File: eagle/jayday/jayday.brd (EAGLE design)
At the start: 120 x 80 mm, 35 parts, among them IC1 TPS2115, X1 2X5_1.27MM, X17 DX2R005HN2E700

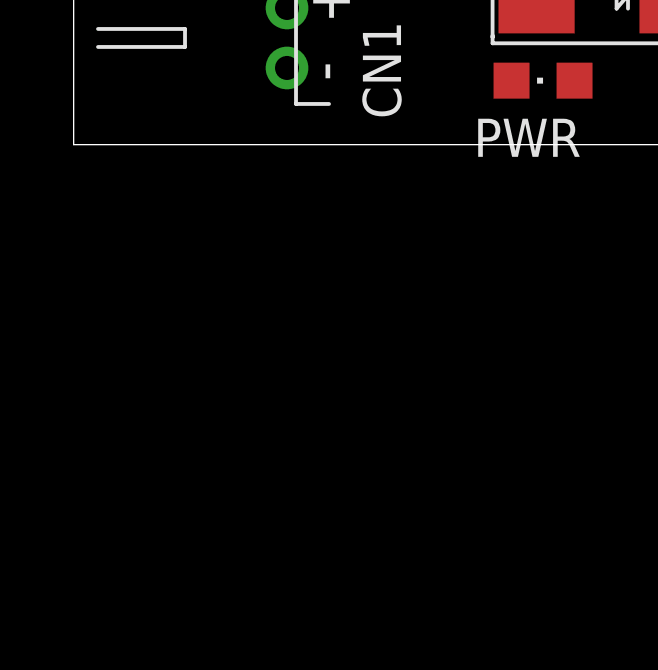
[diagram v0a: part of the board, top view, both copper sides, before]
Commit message: added board with sim900
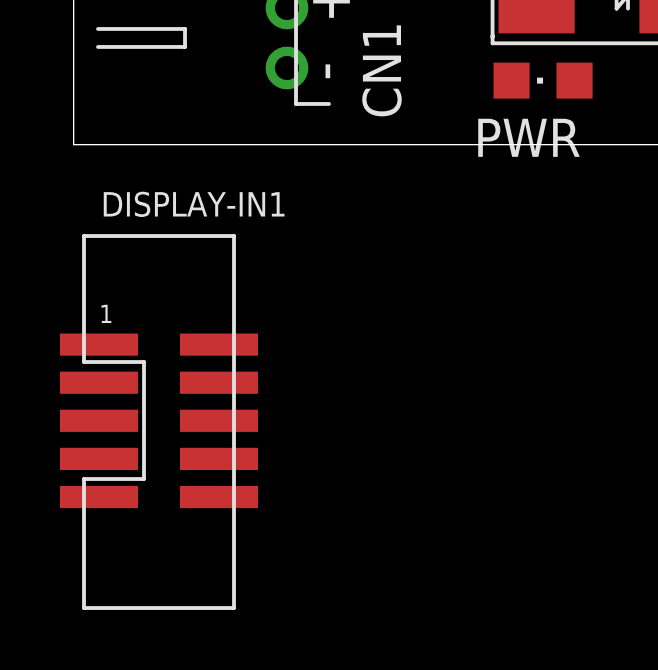
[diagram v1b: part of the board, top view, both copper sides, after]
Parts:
- added DISPLAY-IN1: 2X5_1.27MM, GHI:2X5_1.27MM
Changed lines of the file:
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@@
 <layer number="17" name="Pads" color="2" fill="1" visible="yes" active="yes"/>
 <layer number="18" name="Vias" color="2" fill="1" visible="yes" active="yes"/>
-<layer number="19" name="Unrouted" color="6" fill="1" visible="yes" active="yes"/>
+<layer number="19" name="Unrouted" color="6" fill="1" visible="no" active="yes"/>
 <layer number="20" name="Dimension" color="15" fill="1" visible="yes" active="yes"/>
 <layer number="21" name="tPlace" color="7" fill="1" visible="yes" active="yes"/>
@@
 <element name="PWR2" library="led" package="CHIPLED_0805" value="" x="27.7368" y="57.6072"/>
 <element name="R10" library="rcl" package="R0603" value="1K" x="33.4264" y="51.9176"/>
+<element name="DISPLAY-IN1" library="GHI" package="2X5_1.27MM" value="2X5_1.27MM" x="2.8448" y="-9.2456"/>
 </elements>
 <signals>
